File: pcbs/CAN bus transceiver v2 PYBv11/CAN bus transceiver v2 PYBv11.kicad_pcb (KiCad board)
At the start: 2 copper layers, 30.5 x 15.2 mm, 11 parts, among them P1 CONN_01X06, P2 CONN_01X02, P3 CONN_01X02, P4 CONN_01X06, U1 TCAN337GDR, U2 TCAN337GDR

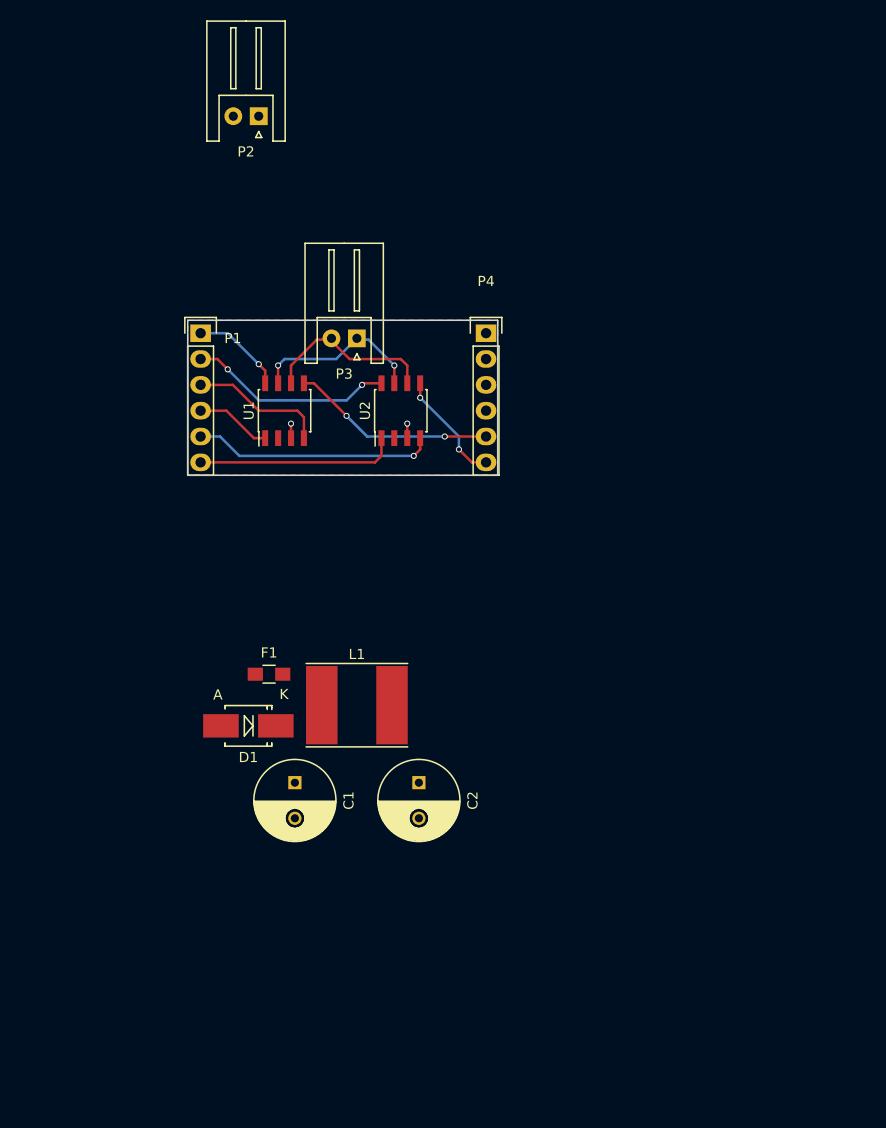
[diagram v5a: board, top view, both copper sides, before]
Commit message: can: added components for LM3489 wiring
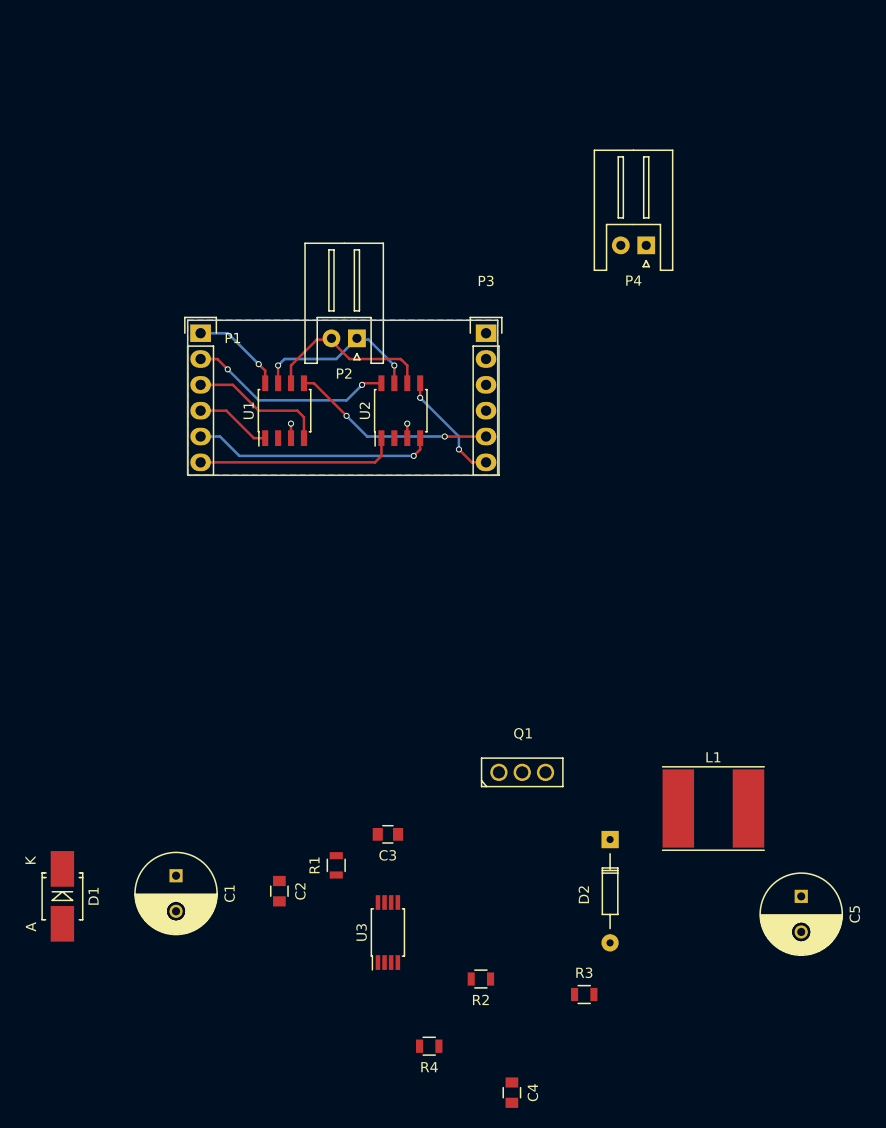
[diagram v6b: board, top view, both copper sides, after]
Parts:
- removed F1: FUSE, Resistors_SMD:R_0805_HandSoldering
- added C3: C, Capacitors_SMD:C_0805, F.Cu at (101.6, 140.7)
- added C4: C, Capacitors_SMD:C_0805, F.Cu at (113.8, 166.1)
- added C5: CP1, Capacitors_ThroughHole:C_Radial_D8_L11.5_P3.5, F.Cu at (142.2, 146.8)
- added D2: D_Schottky, Diodes_ThroughHole:Diode_DO-35_SOD27_Horizontal_RM10, F.Cu at (123.4, 141.2)
- added Q1: Q_PMOS_SGD, TO_SOT_Packages_THT:SOT126_SOT32_Housing_Vertical, F.Cu at (114.8, 134.6)
- added R1: R, Resistors_SMD:R_0805, F.Cu at (96.5, 143.8)
- added R2: R, Resistors_SMD:R_0805, F.Cu at (110.7, 154.9)
- added R3: R, Resistors_SMD:R_0805, F.Cu at (120.9, 156.5)
- added R4: R, Resistors_SMD:R_0805, F.Cu at (105.7, 161.5)
- added U3: LM3489, Housings_SSOP:TSSOP-8_4.4x3mm_Pitch0.65mm, F.Cu at (101.6, 150.4)
- C2: value CP1 -> C; footprint Capacitors_ThroughHole:C_Radial_D8_L11.5_P3.5 -> Capacitors_SMD:C_0805
- P3: value CONN_01X02 -> CONN_01X06; footprint Connectors_JST:JST_XH_S02B-XH-A_02x2.50mm_Angled -> Pin_Headers:Pin_Header_Straight_1x06
- P4: value CONN_01X06 -> CONN_01X02; footprint Pin_Headers:Pin_Header_Straight_1x06 -> Connectors_JST:JST_XH_S02B-XH-A_02x2.50mm_Angled
- moved L1 36.5 mm to (133.6, 138.2)
- moved D1 24.8 mm to (69.6, 146.8), turned to 270 degrees
- moved P2 23.9 mm to (98.6, 91.9)
- moved P4 18.0 mm to (127.0, 82.8), turned to 180 degrees
- moved C2 17.4 mm to (90.9, 146.3)
- moved C1 14.8 mm to (80.8, 144.8)
- moved P3 12.7 mm to (111.3, 91.4), turned to 0 degrees
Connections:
- C1 pad 1: Net-(C1-Pad1) -> +12V
- C2 pad 1: Net-(C2-Pad1) -> +12V
- D1 pad 1: Net-(C1-Pad1) -> +12V
- L1 pad 1: Net-(C1-Pad1) -> Net-(D2-Pad1)
- L1 pad 2: Net-(C2-Pad1) -> +5V
- P2 pad 1: +12V -> Net-(P2-Pad1)
- P2 pad 2: GND -> Net-(P2-Pad2)
- P3 pad 1: Net-(P3-Pad1) -> (no net)
- P3 pad 2: Net-(P3-Pad2) -> +3V3
- P4 pad 1: (no net) -> +12V
- P4 pad 2: +3V3 -> GND
- U1 pad 5: Net-(P4-Pad5) -> Net-(P3-Pad5)
- U1 pad 6: Net-(P3-Pad2) -> Net-(P2-Pad2)
- U1 pad 7: Net-(P3-Pad1) -> Net-(P2-Pad1)
- U2 pad 5: Net-(P4-Pad6) -> Net-(P3-Pad6)
- U2 pad 6: Net-(P3-Pad2) -> Net-(P2-Pad2)
- U2 pad 7: Net-(P3-Pad1) -> Net-(P2-Pad1)
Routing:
- net Net-(P4-Pad5): track 20.0 -> 0.00 mm, vias 2 -> 0
- net Net-(P3-Pad5): track 0.00 -> 20.0 mm, vias 0 -> 2
- net Net-(P3-Pad2): track 17.0 -> 0.00 mm
- net Net-(P2-Pad2): track 0.00 -> 17.0 mm
- net Net-(P2-Pad1): track 0.00 -> 17.0 mm, vias 0 -> 2
- net Net-(P3-Pad1): track 17.0 -> 0.00 mm, vias 2 -> 0
- net Net-(P4-Pad6): track 11.2 -> 0.00 mm, vias 2 -> 0
- net Net-(P3-Pad6): track 0.00 -> 11.2 mm, vias 0 -> 2

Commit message: can: placing LM3489 components on board
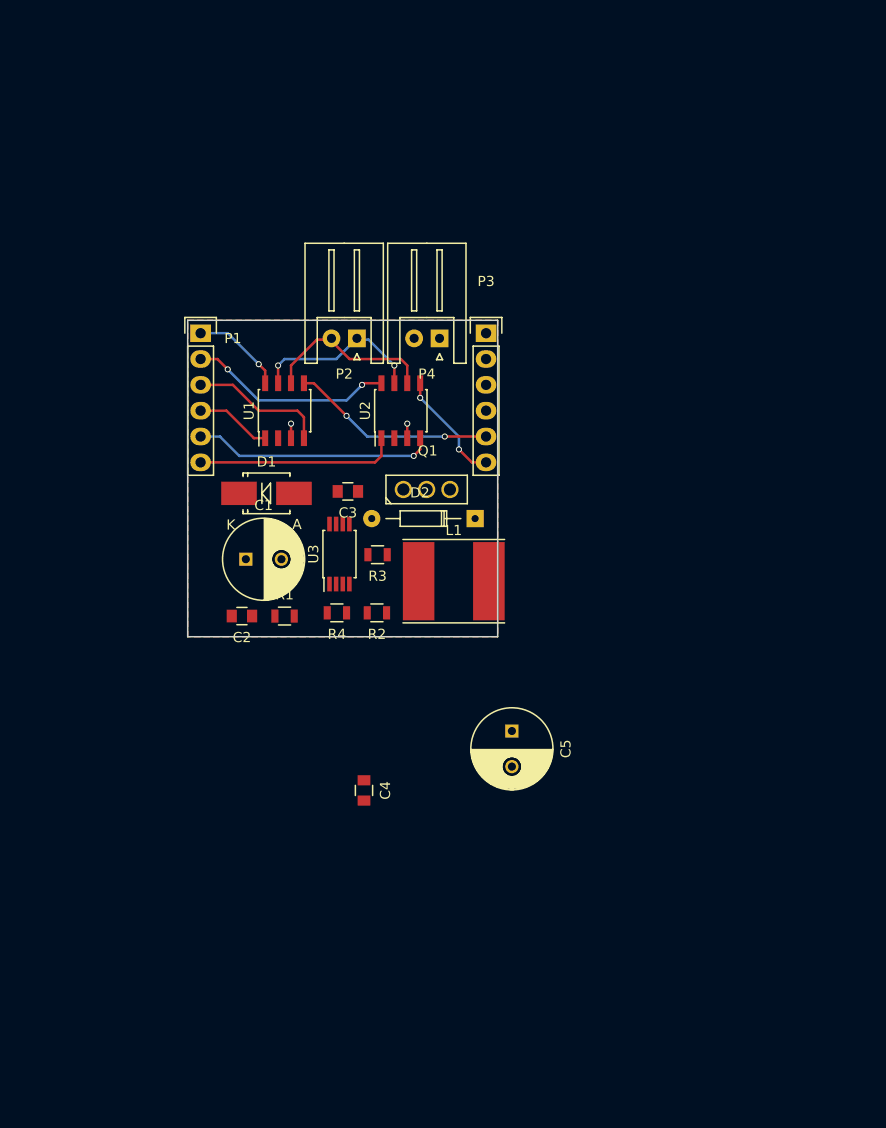
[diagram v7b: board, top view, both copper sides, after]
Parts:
- moved R3 47.8 mm to (100.6, 113.2), turned to 180 degrees
- moved D1 44.4 mm to (89.7, 107.2), turned to 0 degrees
- moved R4 43.6 mm to (96.6, 118.9)
- moved U3 37.5 mm to (96.8, 113.2)
- moved R2 37.4 mm to (100.5, 118.9)
- moved D2 34.2 mm to (110.2, 109.7), turned to 180 degrees
- moved C3 33.9 mm to (97.7, 107.0)
- moved L1 33.9 mm to (108.1, 115.8)
- moved C4 33.1 mm to (99.3, 136.4)
- moved C5 32.8 mm to (113.8, 130.6)
- moved C1 31.9 mm to (87.6, 113.7), turned to 0 degrees
- moved Q1 29.4 mm to (105.4, 106.8)
- moved C2 27.3 mm to (87.2, 119.3), turned to 180 degrees
- moved R1 25.0 mm to (91.4, 119.3), turned to 0 degrees
- moved P4 22.3 mm to (106.7, 91.9)
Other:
- board size 30.5 x 15.2 mm -> 30.5 x 31.1 mm

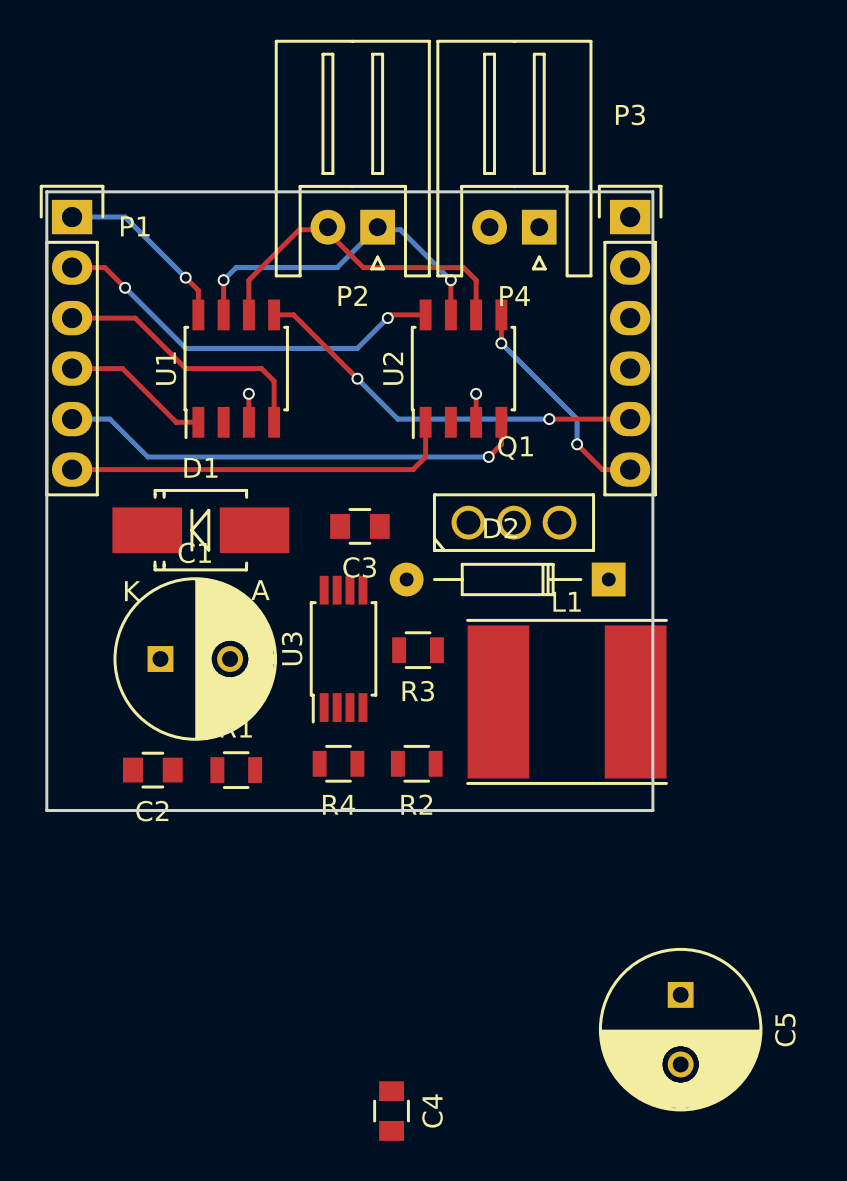
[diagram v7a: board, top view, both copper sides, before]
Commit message: can: placing LM3489 components on board
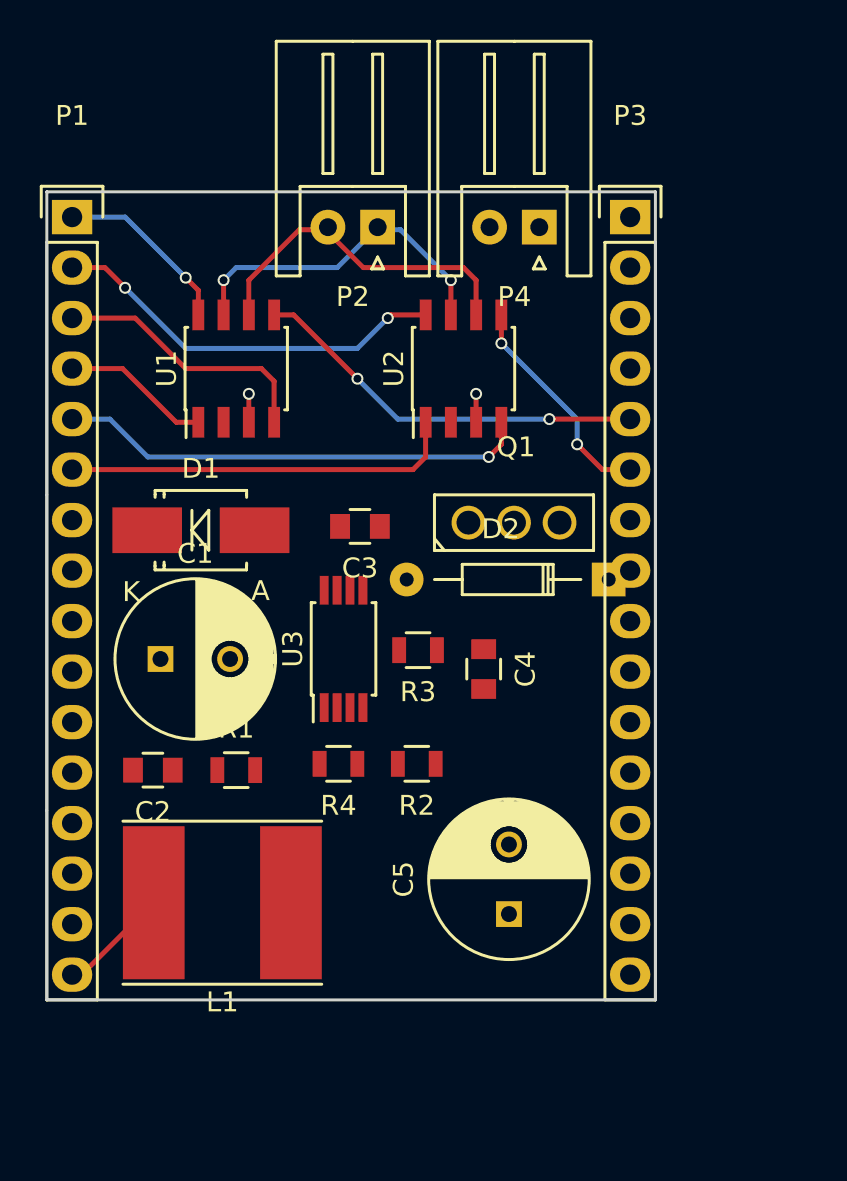
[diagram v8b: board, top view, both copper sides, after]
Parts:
- P1, P3: value CONN_01X06 -> CONN_01X16; footprint Pin_Headers:Pin_Header_Straight_1x06 -> Pin_Headers:Pin_Header_Straight_1x16
- moved C4 22.7 mm to (103.9, 114.2)
- moved L1 20.1 mm to (90.7, 125.9), turned to 180 degrees
- moved C5 9.54 mm to (105.2, 126.5), turned to 90 degrees
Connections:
- P3 pad 1: (no net) -> +5V
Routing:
- net +5V: track 0.00 -> 5.61 mm
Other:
- board size 30.5 x 31.1 mm -> 30.6 x 40.6 mm
